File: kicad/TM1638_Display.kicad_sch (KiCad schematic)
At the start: 0 parts

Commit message: layout - 7seg display
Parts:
- added U8, U9: FJ2481CH, project footprints:7-Seg-CC28-FJ2481CH, symbol Project_Library:7-Seg-CC28-FJ2481CH
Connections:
- new net: U9.2 (d), U9.7 (NA)
- new net: U8.2 (d), U8.7 (NA)
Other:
- note added: "Populate with 2.54mm machined female headers"

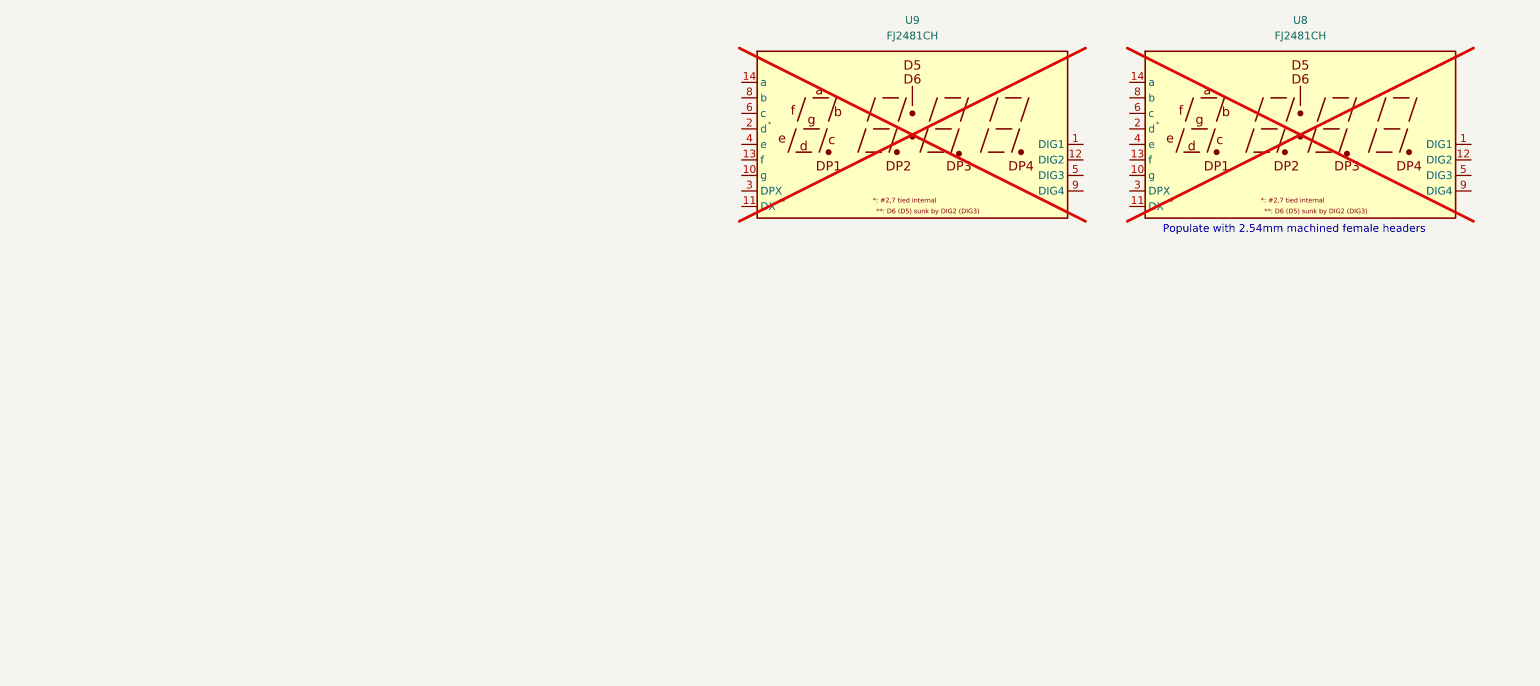
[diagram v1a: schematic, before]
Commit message: layout - footprints update - may have corrupted kicad_sch project lib
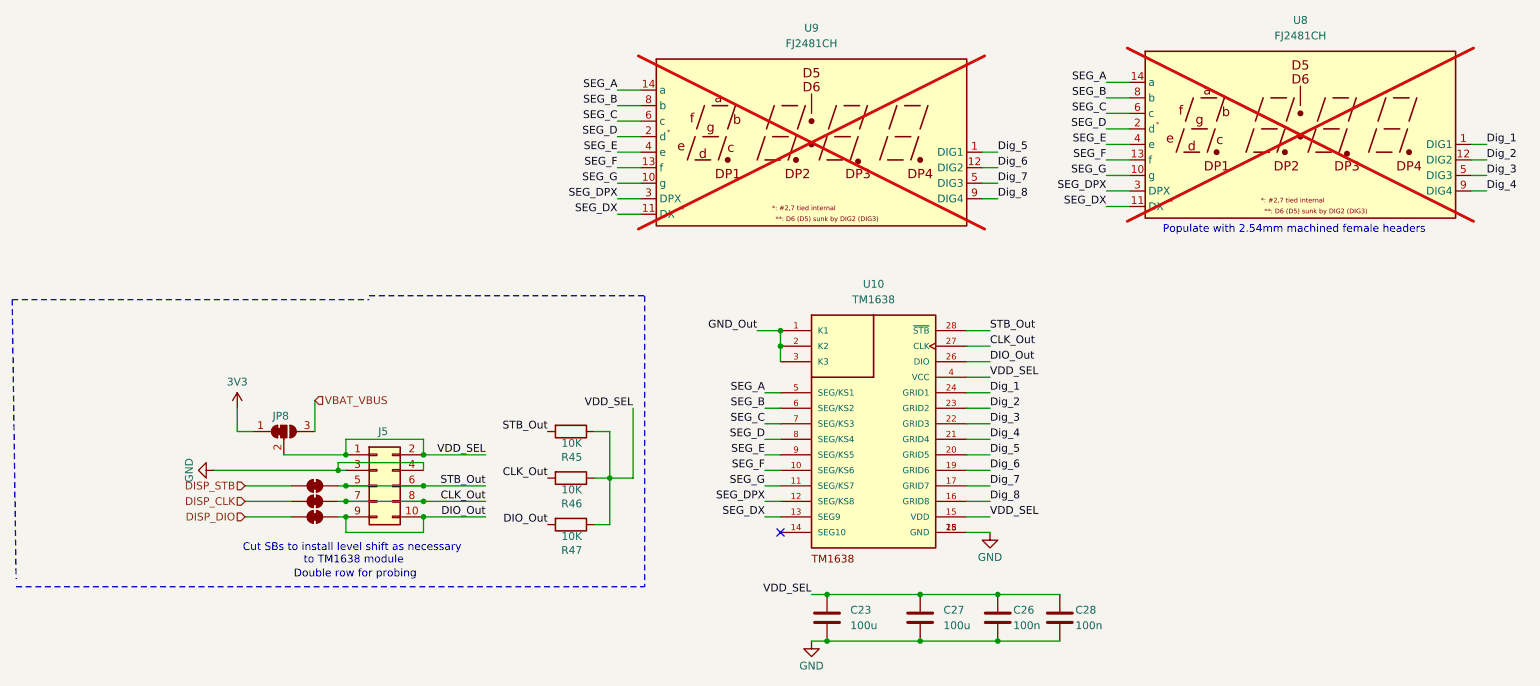
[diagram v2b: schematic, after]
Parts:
- added C23, C27: 100u, Capacitor_SMD:C_1206_3216Metric, symbol Device:C
- added C26, C28: 100n, Capacitor_SMD:C_0603_1608Metric_Pad1.08x0.95mm_HandSolder, symbol Device:C
- added J5: Conn_02x05_Counter_Clockwise, Connector_PinHeader_2.54mm:PinHeader_2x05_P2.54mm_Vertical, symbol Connector_Generic:Conn_02x05_Odd_Even
- added JP16, JP17, JP18: SolderJumper_2_Bridged, Jumper:SolderJumper-2_P1.3mm_Bridged_RoundedPad1.0x1.5mm, symbol Jumper:SolderJumper_2_Bridged
- added JP8: SolderJumper_3_Bridged12, Jumper:SolderJumper-3_P1.3mm_Bridged12_RoundedPad1.0x1.5mm, symbol Jumper:SolderJumper_3_Bridged12
- added R45, R46, R47: 10K, Resistor_SMD:R_0805_2012Metric_Pad1.20x1.40mm_HandSolder, symbol Device:R
- added U10: TM1638, project footprints:SOIC127P1041X265-28N, symbol Project_Library:TM1638
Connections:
- net Dig_5: now reaches U9.1 (DIG1)
- net Dig_5: now also U10.20 (GRID5)
- net SEG_G: now reaches U9.10 (g)
- net SEG_G: now also U8.10 (g), U10.11 (SEG/KS7)
- net SEG_DX: now reaches U9.11 (DX)
- net SEG_DX: now also U8.11 (DX), U10.13 (SEG9)
- net Dig_6: now reaches U9.12 (DIG2)
- net Dig_6: now also U10.19 (GRID6)
- net SEG_F: now reaches U9.13 (f)
- net SEG_F: now also U8.13 (f), U10.10 (SEG/KS6)
- net SEG_A: now reaches U9.14 (a)
- net SEG_A: now also U8.14 (a), U10.5 (SEG/KS1)
- net SEG_D: now reaches U9.2 (d), U9.7 (NA)
- net SEG_D: now also U8.2 (d), U8.7 (NA), U10.8 (SEG/KS4)
- net SEG_DPX: now reaches U9.3 (DPX)
- net SEG_DPX: now also U8.3 (DPX), U10.12 (SEG/KS8)
- net SEG_E: now reaches U9.4 (e)
- net SEG_E: now also U8.4 (e), U10.9 (SEG/KS5)
- net Dig_7: now reaches U9.5 (DIG3)
- net Dig_7: now also U10.17 (GRID7)
- net SEG_C: now reaches U9.6 (c)
- net SEG_C: now also U8.6 (c), U10.7 (SEG/KS3)
- net SEG_B: now reaches U9.8 (b)
- net SEG_B: now also U8.8 (b), U10.6 (SEG/KS2)
- net Dig_8: now reaches U9.9 (DIG4)
- net Dig_8: now also U10.16 (GRID8)
- net Dig_1: now reaches U8.1 (DIG1)
- net Dig_1: now also U10.24 (GRID1)
- net Dig_2: now reaches U8.12 (DIG2)
- net Dig_2: now also U10.23 (GRID2)
- net Dig_3: now reaches U8.5 (DIG3)
- net Dig_3: now also U10.22 (GRID3)
- net Dig_4: now reaches U8.9 (DIG4)
- net Dig_4: now also U10.21 (GRID4)
- new net 3V3: JP8.1 (A)
- new net CLK_Out: J5.7 (Pin_7), J5.8 (Pin_8), JP17.1 (A), R46.2, U10.27 (CLK)
- new net DIO_Out: J5.10 (Pin_10), J5.9 (Pin_9), JP18.1 (A), R47.2, U10.26 (DIO)
- new net DISP_CLK: JP17.2 (B)
- new net DISP_DIO: JP18.2 (B)
- new net DISP_STB: JP16.2 (B)
- new net GND: C23.2, C26.2, C27.2, C28.2, J5.3 (Pin_3), J5.4 (Pin_4), U10.18 (GND), U10.25 (GND)
- new net GND_Out: U10.1 (K1), U10.2 (K2), U10.3 (K3)
- new net STB_Out: J5.5 (Pin_5), J5.6 (Pin_6), JP16.1 (A), R45.2, U10.28 (~{STB})
- new net VBAT_VBUS: JP8.3 (B)
- new net VDD_SEL: C23.1, C26.1, C27.1, C28.1, J5.1 (Pin_1), J5.2 (Pin_2), JP8.2 (C), R45.1, R46.1, R47.1, U10.15 (VDD), U10.4 (VCC)
- no-connect marks 0 -> 1
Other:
- note added: "Cut SBs to install level shift as necessary"
- note added: "Double row for probing"
- note added: "to TM1638 module"
- moved on the sheet: U9

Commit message: changed usb port, prepare first bom export
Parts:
- C26, C28, J5, U10: Lab_In_Stock (none) -> Y
- U8, U9: Lab_In_Stock (none) -> Y; Stock_In_Lab Y -> (none)
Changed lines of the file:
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@@
+			)
+		)
+		(property "Lab_In_Stock" "Y"
+			(at 179.07 85.09 0)
+			(effects
+				(font
+					(size 1.27 1.27)
+				)
+				(hide yes)
 			)
 		)
@@
 			)
 		)
+		(property "Lab_In_Stock" "Y"
+			(at 199.39 114.3 0)
+			(effects
+				(font
+					(size 1.27 1.27)
+				)
+				(hide yes)
+			)
+		)
 		(pin "2"
 		)
@@
 		)
 		(property "Subsystem" "06-MCU-IO"
+			(at 97.79 92.71 0)
+			(effects
+				(font
+					(size 1.27 1.27)
+				)
+				(hide yes)
+			)
+		)
+		(property "Lab_In_Stock" "Y"
 			(at 97.79 92.71 0)
 			(effects
@@
 			)
 		)
-		(property "Stock_In_Lab" "Y"
+		(property "Lab_In_Stock" "Y"
 			(at 168.91 35.56 0)
 			(effects
@@
 			)
 		)
+		(property "Lab_In_Stock" "Y"
+			(at 209.55 114.3 0)
+			(effects
+				(font
+					(size 1.27 1.27)
+				)
+				(hide yes)
+			)
+		)
 		(pin "2"
 		)
@@
 			)
 		)
-		(property "Stock_In_Lab" "Y"
+		(property "Lab_In_Stock" "Y"
 			(at 248.92 34.29 0)
 			(effects

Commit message: DRC to zero errors - still need to check FPs
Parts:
- added R49: 10K, Resistor_SMD:R_0805_2012Metric_Pad1.20x1.40mm_HandSolder, symbol Device:R
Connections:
- net GND: now also R49.2
- net GND_Out: no longer names the net of U10.1 (K1), U10.2 (K2), U10.3 (K3)
- net GND_Out: now also R49.1
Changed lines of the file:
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@@
+	(wire
+		(pts
+			(xy 151.13 67.31) (xy 152.4 67.31)
+		)
+		(stroke
+			(width 0)
+			(type default)
+		)
+	)
 	(wire
 		(pts
@@
 		)
 	)
-	(label "GND_Out"
-		(at 160.02 67.31 180)
-		(effects
-			(font
-				(size 1.27 1.27)
-			)
-			(justify right bottom)
-		)
-	)
 	(label "SEG_C"
 		(at 217.17 31.75 180)
@@
 			)
 			(justify right)
+		)
+	)
+	(symbol
+		(lib_id "Device:R")
+		(at 156.21 67.31 270)
+		(unit 1)
+		(exclude_from_sim no)
+		(in_bom yes)
+		(on_board yes)
+		(dnp no)
+		(property "Reference" "R49"
+			(at 156.337 71.501 90)
+			(effects
+				(font
+					(size 1.27 1.27)
+				)
+			)
+		)
+		(property "Value" "10K"
+			(at 156.337 69.215 90)
+			(effects
+				(font
+					(size 1.27 1.27)
+				)
+			)
+		)
+		(property "Footprint" "Resistor_SMD:R_0805_2012Metric_Pad1.20x1.40mm_HandSolder"
+			(at 156.21 65.532 90)
+			(effects
+				(font
+					(size 1.27 1.27)
+				)
+				(hide yes)
+			)
+		)
+		(property "Datasheet" "~"
+			(at 156.21 67.31 0)
+			(effects
+				(font
+					(size 1.27 1.27)
+				)
+				(hide yes)
+			)
+		)
+		(property "Description" "Resistor"
+			(at 156.21 67.31 0)
+			(effects
+				(font
+					(size 1.27 1.27)
+				)
+				(hide yes)
+			)
+		)
+		(property "Subsystem" "06-MCU-IO"
+			(at 156.21 67.31 0)
+			(effects
+				(font
+					(size 1.27 1.27)
+				)
+				(hide yes)
+			)
+		)
+		(property "MPN" "(Generic)"
+			(at 156.21 67.31 0)
+			(effects
+				(font
+					(size 1.27 1.27)
+				)
+				(hide yes)
+			)
+		)
+		(property "Manufacturer" "(Generic)"
+			(at 156.21 67.31 90)
+			(effects
+				(font
+					(size 1.27 1.27)
+				)
+				(hide yes)
+			)
+		)
+		(property "Supplier 1" "(Generic)"
+			(at 156.21 67.31 90)
+			(effects
+				(font
+					(size 1.27 1.27)
+				)
+				(hide yes)
+			)
+		)
+		(property "Package" "0805"
+			(at 156.21 67.31 90)
+			(effects
+				(font
+					(size 1.27 1.27)
+				)
+				(hide yes)
+			)
+		)
+		(pin "1"
+		)
+		(pin "2"
+		)
+		(instances
+			(project "10k-Hour-Timer-RP2040"
+				(path "/9d26b66f-2a94-42e5-8460-016e0bf95186/892e3d5c-3b02-4812-a25c-8412b58cd20c"
+					(reference "R49")
+					(unit 1)
+				)
+			)
 		)
 	)
@@
 					(unit 1)
 				)
+			)
+		)
+	)
+	(symbol
+		(lib_id "power:GND")
+		(at 151.13 67.31 0)
+		(unit 1)
+		(exclude_from_sim no)
+		(in_bom yes)
+		(on_board yes)
+		(dnp no)
+		(property "Reference" "#PWR064"
+			(at 151.13 73.66 0)
+			(effects
+				(font
+					(size 1.27 1.27)
+				)
+				(hide yes)
+			)
+		)
+		(property "Value" "GND"
+			(at 151.13 71.374 0)
+			(effects
+				(font
+					(size 1.27 1.27)
+				)
+			)
+		)
+		(property "Footprint" ""
+			(at 151.13 67.31 0)
+			(effects
+				(font
+					(size 1.27 1.27)
+				)
+				(hide yes)
+			)
+		)
+		(property "Datasheet" ""
+			(at 151.13 67.31 0)
+			(effects
+				(font
+					(size 1.27 1.27)
+				)
+				(hide yes)
+			)
+		)
+		(property "Description" "Power symbol creates a global label with name \"GND\" , ground"
+			(at 151.13 67.31 0)
+			(effects
+				(font
+					(size 1.27 1.27)
+				)
+				(hide yes)
+			)
+		)
+		(pin "1"
+		)
+		(instances
+			(project "10k-Hour-Timer-RP2040"
+				(path "/9d26b66f-2a94-42e5-8460-016e0bf95186/892e3d5c-3b02-4812-a25c-8412b58cd20c"
+					(reference "#PWR064")
+					(unit 1)
+				)

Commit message: production files for PCBWay initial - BOM manually edited for PCBA
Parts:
- J5: now not fitted
- U10, U8, U9: Subsystem (none) -> 08-LED
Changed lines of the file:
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@@
+			)
+		)
+		(property "Subsystem" "08-LED"
+			(at 179.07 85.09 0)
+			(effects
+				(font
+					(size 1.27 1.27)
+				)
+				(hide yes)
 			)
 		)
@@
 		(in_bom yes)
 		(on_board yes)
-		(dnp no)
+		(dnp yes)
 		(property "Reference" "J5"
 			(at 98.806 83.82 0)
@@
 			)
 		)
+		(property "Subsystem" "08-LED"
+			(at 168.91 35.56 0)
+			(effects
+				(font
+					(size 1.27 1.27)
+				)
+				(hide yes)
+			)
+		)
 		(pin "12"
 		)
@@
 			(at 248.92 34.29 0)
 			(effects
+				(font
+					(size 1.27 1.27)
+				)
+				(hide yes)
+			)
+		)
+		(property "Subsystem" "08-LED"
+			(at 248.92 34.29 0)
+			(effects
